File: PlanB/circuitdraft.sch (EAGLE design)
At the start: 22 parts, among them Y1 CY16BPS

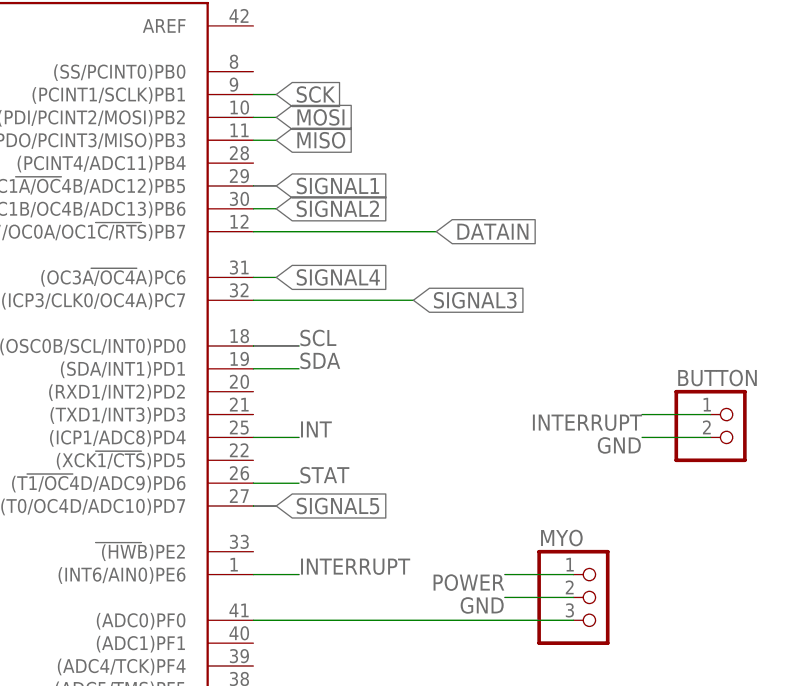
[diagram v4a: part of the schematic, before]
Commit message: changed some pins to match arduino pins
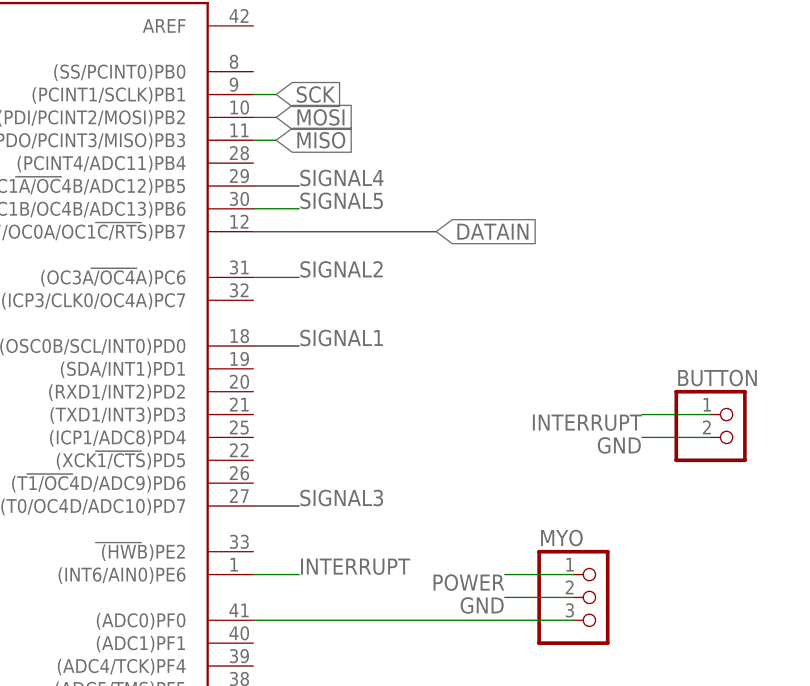
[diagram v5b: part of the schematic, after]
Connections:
- removed net INT: U$1.(ICP1/ADC8)PD4
- removed net SCL: U$1.(OSC0B/SCL/INT0)PD0
- removed net SDA: U$1.(SDA/INT1)PD1
- removed net STAT: U$1.(T1/OC4D/ADC9)PD6
- net SIGNAL1: now also U$1.(OSC0B/SCL/INT0)PD0; no longer U$1.(PCINT5/OC1A/OC4B/ADC12)PB5
- net SIGNAL2: now also U$1.(OC3A/OC4A)PC6; no longer U$1.(PCINT6/OC1B/OC4B/ADC13)PB6
- net SIGNAL3: now also U$1.(T0/OC4D/ADC10)PD7; no longer U$1.(ICP3/CLK0/OC4A)PC7
- net SIGNAL4: now also U$1.(PCINT5/OC1A/OC4B/ADC12)PB5; no longer U$1.(OC3A/OC4A)PC6
- net SIGNAL5: now also U$1.(PCINT6/OC1B/OC4B/ADC13)PB6; no longer U$1.(T0/OC4D/ADC10)PD7
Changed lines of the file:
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@@
 <net name="SIGNAL1" class="0">
-<segment>
-<pinref part="U$1" gate="G$1" pin="(PCINT5/OC1A/OC4B/ADC12)PB5"/>
-<wire x1="195.58" y1="165.1" x2="198.12" y2="165.1" width="0.1524" layer="91"/>
-<label x="198.12" y="165.1" size="1.778" layer="95" xref="yes"/>
-</segment>
 <segment>
 <pinref part="SERVO1" gate="A" pin="1"/>
@@
 <label x="195.58" y="223.52" size="1.778" layer="95" rot="R180"/>
 </segment>
+<segment>
+<pinref part="U$1" gate="G$1" pin="(OSC0B/SCL/INT0)PD0"/>
+<wire x1="195.58" y1="147.32" x2="200.66" y2="147.32" width="0.1524" layer="91"/>
+<label x="200.66" y="147.32" size="1.778" layer="95"/>
+</segment>
 </net>
 <net name="SIGNAL2" class="0">
-<segment>
-<pinref part="U$1" gate="G$1" pin="(PCINT6/OC1B/OC4B/ADC13)PB6"/>
-<wire x1="195.58" y1="162.56" x2="198.12" y2="162.56" width="0.1524" layer="91"/>
-<label x="198.12" y="162.56" size="1.778" layer="95" xref="yes"/>
-</segment>
 <segment>
 <pinref part="SERVO2" gate="A" pin="1"/>
@@
 <label x="210.82" y="231.14" size="1.778" layer="95"/>
 </segment>
+<segment>
+<pinref part="U$1" gate="G$1" pin="(OC3A/OC4A)PC6"/>
+<wire x1="195.58" y1="154.94" x2="200.66" y2="154.94" width="0.1524" layer="91"/>
+<label x="200.66" y="154.94" size="1.778" layer="95"/>
+</segment>
 </net>
 <net name="SIGNAL3" class="0">
-<segment>
-<pinref part="U$1" gate="G$1" pin="(ICP3/CLK0/OC4A)PC7"/>
-<wire x1="195.58" y1="152.4" x2="213.36" y2="152.4" width="0.1524" layer="91"/>
-<label x="213.36" y="152.4" size="1.778" layer="95" xref="yes"/>
-</segment>
 <segment>
 <pinref part="SERVO3" gate="A" pin="1"/>
@@
 <label x="223.52" y="231.14" size="1.778" layer="95"/>
 </segment>
+<segment>
+<pinref part="U$1" gate="G$1" pin="(T0/OC4D/ADC10)PD7"/>
+<wire x1="195.58" y1="129.54" x2="200.66" y2="129.54" width="0.1524" layer="91"/>
+<label x="200.66" y="129.54" size="1.778" layer="95"/>
+</segment>
 </net>
 <net name="SIGNAL4" class="0">
-<segment>
-<pinref part="U$1" gate="G$1" pin="(OC3A/OC4A)PC6"/>
-<wire x1="195.58" y1="154.94" x2="198.12" y2="154.94" width="0.1524" layer="91"/>
-<label x="198.12" y="154.94" size="1.778" layer="95" xref="yes"/>
-</segment>
 <segment>
 <pinref part="SERVO4" gate="A" pin="1"/>
@@
 <label x="236.22" y="231.14" size="1.778" layer="95"/>
 </segment>
+<segment>
+<pinref part="U$1" gate="G$1" pin="(PCINT5/OC1A/OC4B/ADC12)PB5"/>
+<wire x1="195.58" y1="165.1" x2="200.66" y2="165.1" width="0.1524" layer="91"/>
+<label x="200.66" y="165.1" size="1.778" layer="95"/>
+</segment>
 </net>
 <net name="SIGNAL5" class="0">
-<segment>
-<pinref part="U$1" gate="G$1" pin="(T0/OC4D/ADC10)PD7"/>
-<wire x1="195.58" y1="129.54" x2="198.12" y2="129.54" width="0.1524" layer="91"/>
-<label x="198.12" y="129.54" size="1.778" layer="95" xref="yes"/>
-</segment>
 <segment>
 <pinref part="SERVO5" gate="A" pin="1"/>
@@
 <wire x1="248.92" y1="223.52" x2="248.92" y2="231.14" width="0.1524" layer="91"/>
 <label x="248.92" y="231.14" size="1.778" layer="95"/>
+</segment>
+<segment>
+<pinref part="U$1" gate="G$1" pin="(PCINT6/OC1B/OC4B/ADC13)PB6"/>
+<wire x1="195.58" y1="162.56" x2="200.66" y2="162.56" width="0.1524" layer="91"/>
+<label x="200.66" y="162.56" size="1.778" layer="95"/>
 </segment>
 </net>
@@
 </segment>
 </net>
-<net name="SCL" class="0">
-<segment>
-<pinref part="U$1" gate="G$1" pin="(OSC0B/SCL/INT0)PD0"/>
-<wire x1="195.58" y1="147.32" x2="200.66" y2="147.32" width="0.1524" layer="91"/>
-<label x="200.66" y="147.32" size="1.778" layer="95"/>
-</segment>
-</net>
-<net name="SDA" class="0">
-<segment>
-<pinref part="U$1" gate="G$1" pin="(SDA/INT1)PD1"/>
-<wire x1="195.58" y1="144.78" x2="200.66" y2="144.78" width="0.1524" layer="91"/>
-<label x="200.66" y="144.78" size="1.778" layer="95"/>
-</segment>
-</net>
-<net name="INT" class="0">
-<segment>
-<pinref part="U$1" gate="G$1" pin="(ICP1/ADC8)PD4"/>
-<wire x1="195.58" y1="137.16" x2="200.66" y2="137.16" width="0.1524" layer="91"/>
-<label x="200.66" y="137.16" size="1.778" layer="95"/>
-</segment>
-</net>
-<net name="STAT" class="0">
-<segment>
-<pinref part="U$1" gate="G$1" pin="(T1/OC4D/ADC9)PD6"/>
-<wire x1="195.58" y1="132.08" x2="200.66" y2="132.08" width="0.1524" layer="91"/>
-<label x="200.66" y="132.08" size="1.778" layer="95"/>
-</segment>
-</net>

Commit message: updated
rotated servo ports
removed unnecessary USB things
moved some things around
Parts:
- removed C1: 1 uF, rcl:C-US050-024X044
- removed R1, R2: 22 Ohms, rcl:R-US_0207/10
- USB: device pinhead:PINHD-1X4 -> pinhead:PINHD-1X2
- renumbered BUTTON to BUT, REGIN to IREG, REGOUT to OREG, SERVO1 to S1, SERVO2 to S2, SERVO3 to S3, SERVO4 to S4, SERVO5 to S5
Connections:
- removed net D+: R1.1, USB.2
- removed net D-: R2.1, USB.3
- removed net N$2: R2.2, U$1.D-
- removed net N$3: C1.1, U$1.UCAP
- removed net N$4: R1.2, U$1.D+
- net BIGPOWER: now also MYO.1
- net GND: now also USB.2; no longer C1.2, USB.4
- net POWER: no longer MYO.1

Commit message: added tx/rx and moved a few things
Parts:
- added IO: (no value), pinhead:PINHD-1X3
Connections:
- new net RX: IO.1, U$1.(RXD1/INT2)PD2
- new net TX: IO.2, U$1.(TXD1/INT3)PD3
- net GND: now also IO.3
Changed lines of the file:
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@@
 <part name="IREG" library="pinhead" library_urn="urn:adsk.eagle:library:325" deviceset="PINHD-1X4" device="" package3d_urn="urn:adsk.eagle:package:22407/2"/>
 <part name="OREG" library="pinhead" library_urn="urn:adsk.eagle:library:325" deviceset="PINHD-1X4" device="" package3d_urn="urn:adsk.eagle:package:22407/2"/>
+<part name="IO" library="pinhead" library_urn="urn:adsk.eagle:library:325" deviceset="PINHD-1X3" device="" package3d_urn="urn:adsk.eagle:package:22458/2"/>
 </parts>
 <sheets>
@@
 <attribute name="NAME" x="34.29" y="120.015" size="1.778" layer="95"/>
 <attribute name="VALUE" x="34.29" y="104.14" size="1.778" layer="96"/>
+</instance>
+<instance part="IO" gate="A" x="220.98" y="139.7" smashed="yes">
+<attribute name="NAME" x="214.63" y="145.415" size="1.778" layer="95"/>
+<attribute name="VALUE" x="214.63" y="132.08" size="1.778" layer="96"/>
 </instance>
 </instances>
@@
 <label x="274.32" y="187.96" size="1.778" layer="95"/>
 </segment>
+<segment>
+<pinref part="IO" gate="A" pin="3"/>
+<wire x1="218.44" y1="137.16" x2="210.82" y2="137.16" width="0.1524" layer="91"/>
+<label x="205.74" y="137.16" size="1.778" layer="95"/>
+</segment>
 </net>
 <net name="INTERRUPT" class="0">
@@
 </segment>
 </net>
+<net name="RX" class="0">
+<segment>
+<pinref part="U$1" gate="G$1" pin="(RXD1/INT2)PD2"/>
+<wire x1="195.58" y1="142.24" x2="198.12" y2="142.24" width="0.1524" layer="91"/>
+<label x="198.12" y="142.24" size="1.778" layer="95"/>
+</segment>
+<segment>
+<pinref part="IO" gate="A" pin="1"/>
+<wire x1="218.44" y1="142.24" x2="210.82" y2="142.24" width="0.1524" layer="91"/>
+<label x="205.74" y="142.24" size="1.778" layer="95"/>
+</segment>
+</net>
+<net name="TX" class="0">
+<segment>
+<pinref part="U$1" gate="G$1" pin="(TXD1/INT3)PD3"/>
+<wire x1="195.58" y1="139.7" x2="198.12" y2="139.7" width="0.1524" layer="91"/>
+<label x="198.12" y="139.7" size="1.778" layer="95"/>
+</segment>
+<segment>
+<pinref part="IO" gate="A" pin="2"/>
+<wire x1="218.44" y1="139.7" x2="210.82" y2="139.7" width="0.1524" layer="91"/>
+<label x="208.28" y="139.7" size="1.778" layer="95"/>
+</segment>
+</net>
